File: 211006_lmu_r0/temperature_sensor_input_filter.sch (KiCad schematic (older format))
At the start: 4 parts

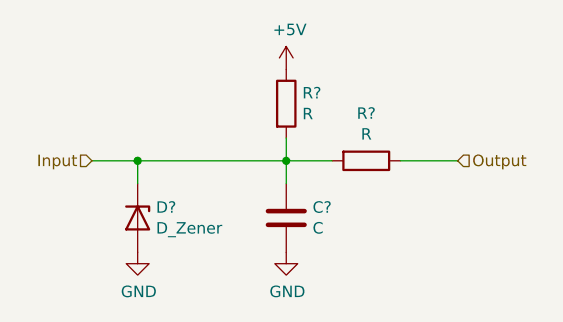
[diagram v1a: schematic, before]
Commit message: Updated BOM and footprints for non-hv components
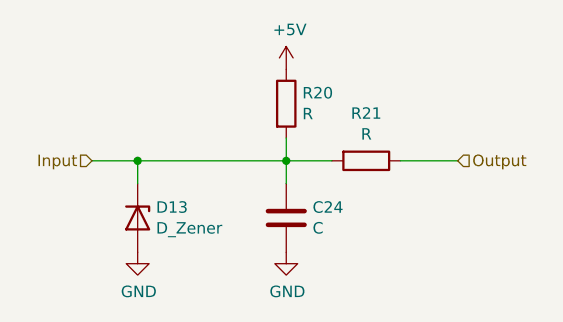
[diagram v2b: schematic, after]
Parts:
- gave numbers to parts that had none: 4
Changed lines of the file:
@@
 $EndDescr
 $Comp
-L Device:R R?
+L Device:R R6
 U 1 1 616C81A3
 P 6250 3350
-AR Path="/6171146A/616C8099/616C81A3" Ref="R?"  Part="1"
-AR Path="/6171146A/616CF5C8/616C81A3" Ref="R?"  Part="1"
-AR Path="/6171146A/616CF706/616C81A3" Ref="R?"  Part="1"
-AR Path="/6171146A/616CF70A/616C81A3" Ref="R?"  Part="1"
-AR Path="/6171146A/616D0104/616C81A3" Ref="R?"  Part="1"
-AR Path="/6171146A/616D0108/616C81A3" Ref="R?"  Part="1"
-AR Path="/6171146A/616D010C/616C81A3" Ref="R?"  Part="1"
-AR Path="/6171146A/616D0110/616C81A3" Ref="R?"  Part="1"
-F 0 "R?" H 6320 3396 50  0000 L CNN
+AR Path="/6171146A/616C8099/616C81A3" Ref="R6"  Part="1"
+AR Path="/6171146A/616CF5C8/616C81A3" Ref="R8"  Part="1"
+AR Path="/6171146A/616CF706/616C81A3" Ref="R10"  Part="1"
+AR Path="/6171146A/616CF70A/616C81A3" Ref="R12"  Part="1"
+AR Path="/6171146A/616D0104/616C81A3" Ref="R14"  Part="1"
+AR Path="/6171146A/616D0108/616C81A3" Ref="R16"  Part="1"
+AR Path="/6171146A/616D010C/616C81A3" Ref="R18"  Part="1"
+AR Path="/6171146A/616D0110/616C81A3" Ref="R20"  Part="1"
+F 0 "R20" H 6320 3396 50  0000 L CNN
 F 1 "R" H 6320 3305 50  0000 L CNN
 F 2 "" V 6180 3350 50  0001 C CNN
@@
 $EndComp
 $Comp
-L Device:R R?
+L Device:R R7
 U 1 1 616C83F1
 P 6600 3600
-AR Path="/6171146A/616C8099/616C83F1" Ref="R?"  Part="1"
-AR Path="/6171146A/616CF5C8/616C83F1" Ref="R?"  Part="1"
-AR Path="/6171146A/616CF706/616C83F1" Ref="R?"  Part="1"
-AR Path="/6171146A/616CF70A/616C83F1" Ref="R?"  Part="1"
-AR Path="/6171146A/616D0104/616C83F1" Ref="R?"  Part="1"
-AR Path="/6171146A/616D0108/616C83F1" Ref="R?"  Part="1"
-AR Path="/6171146A/616D010C/616C83F1" Ref="R?"  Part="1"
-AR Path="/6171146A/616D0110/616C83F1" Ref="R?"  Part="1"
-F 0 "R?" V 6393 3600 50  0000 C CNN
+AR Path="/6171146A/616C8099/616C83F1" Ref="R7"  Part="1"
+AR Path="/6171146A/616CF5C8/616C83F1" Ref="R9"  Part="1"
+AR Path="/6171146A/616CF706/616C83F1" Ref="R11"  Part="1"
+AR Path="/6171146A/616CF70A/616C83F1" Ref="R13"  Part="1"
+AR Path="/6171146A/616D0104/616C83F1" Ref="R15"  Part="1"
+AR Path="/6171146A/616D0108/616C83F1" Ref="R17"  Part="1"
+AR Path="/6171146A/616D010C/616C83F1" Ref="R19"  Part="1"
+AR Path="/6171146A/616D0110/616C83F1" Ref="R21"  Part="1"
+F 0 "R21" V 6393 3600 50  0000 C CNN
 F 1 "R" V 6484 3600 50  0000 C CNN
 F 2 "" V 6530 3600 50  0001 C CNN
@@
 $EndComp
 $Comp
-L Device:C C?
+L Device:C C17
 U 1 1 616C95FD
 P 6250 3850
-AR Path="/6171146A/616C8099/616C95FD" Ref="C?"  Part="1"
-AR Path="/6171146A/616CF5C8/616C95FD" Ref="C?"  Part="1"
-AR Path="/6171146A/616CF706/616C95FD" Ref="C?"  Part="1"
-AR Path="/6171146A/616CF70A/616C95FD" Ref="C?"  Part="1"
-AR Path="/6171146A/616D0104/616C95FD" Ref="C?"  Part="1"
-AR Path="/6171146A/616D0108/616C95FD" Ref="C?"  Part="1"
-AR Path="/6171146A/616D010C/616C95FD" Ref="C?"  Part="1"
-AR Path="/6171146A/616D0110/616C95FD" Ref="C?"  Part="1"
-F 0 "C?" H 6135 3804 50  0000 R CNN
+AR Path="/6171146A/616C8099/616C95FD" Ref="C17"  Part="1"
+AR Path="/6171146A/616CF5C8/616C95FD" Ref="C18"  Part="1"
+AR Path="/6171146A/616CF706/616C95FD" Ref="C19"  Part="1"
+AR Path="/6171146A/616CF70A/616C95FD" Ref="C20"  Part="1"
+AR Path="/6171146A/616D0104/616C95FD" Ref="C21"  Part="1"
+AR Path="/6171146A/616D0108/616C95FD" Ref="C22"  Part="1"
+AR Path="/6171146A/616D010C/616C95FD" Ref="C23"  Part="1"
+AR Path="/6171146A/616D0110/616C95FD" Ref="C24"  Part="1"
+F 0 "C24" H 6135 3804 50  0000 R CNN
 F 1 "C" H 6135 3895 50  0000 R CNN
 F 2 "" H 6288 3700 50  0001 C CNN
@@
 $EndComp
 $Comp
-L power:+5V #PWR?
+L power:+5V #PWR0116
 U 1 1 616CA1AB
 P 6250 3200
-AR Path="/6171146A/616C8099/616CA1AB" Ref="#PWR?"  Part="1"
-AR Path="/6171146A/616CF5C8/616CA1AB" Ref="#PWR?"  Part="1"
-AR Path="/6171146A/616CF706/616CA1AB" Ref="#PWR?"  Part="1"
-AR Path="/6171146A/616CF70A/616CA1AB" Ref="#PWR?"  Part="1"
-AR Path="/6171146A/616D0104/616CA1AB" Ref="#PWR?"  Part="1"
-AR Path="/6171146A/616D0108/616CA1AB" Ref="#PWR?"  Part="1"
-AR Path="/6171146A/616D010C/616CA1AB" Ref="#PWR?"  Part="1"
-AR Path="/6171146A/616D0110/616CA1AB" Ref="#PWR?"  Part="1"
-F 0 "#PWR?" H 6250 3050 50  0001 C CNN
+AR Path="/6171146A/616C8099/616CA1AB" Ref="#PWR0116"  Part="1"
+AR Path="/6171146A/616CF5C8/616CA1AB" Ref="#PWR0119"  Part="1"
+AR Path="/6171146A/616CF706/616CA1AB" Ref="#PWR0122"  Part="1"
+AR Path="/6171146A/616CF70A/616CA1AB" Ref="#PWR0125"  Part="1"
+AR Path="/6171146A/616D0104/616CA1AB" Ref="#PWR0128"  Part="1"
+AR Path="/6171146A/616D0108/616CA1AB" Ref="#PWR0131"  Part="1"
+AR Path="/6171146A/616D010C/616CA1AB" Ref="#PWR0134"  Part="1"
+AR Path="/6171146A/616D0110/616CA1AB" Ref="#PWR0137"  Part="1"
+F 0 "#PWR0137" H 6250 3050 50  0001 C CNN
 F 1 "+5V" H 6265 3373 50  0000 C CNN
 F 2 "" H 6250 3200 50  0001 C CNN
@@
 	6250 3600 6250 3700
 $Comp
-L power:GND #PWR?
+L power:GND #PWR0117
 U 1 1 616CAA95
 P 6250 4000
-AR Path="/6171146A/616C8099/616CAA95" Ref="#PWR?"  Part="1"
-AR Path="/6171146A/616CF5C8/616CAA95" Ref="#PWR?"  Part="1"
-AR Path="/6171146A/616CF706/616CAA95" Ref="#PWR?"  Part="1"
-AR Path="/6171146A/616CF70A/616CAA95" Ref="#PWR?"  Part="1"
-AR Path="/6171146A/616D0104/616CAA95" Ref="#PWR?"  Part="1"
-AR Path="/6171146A/616D0108/616CAA95" Ref="#PWR?"  Part="1"
-AR Path="/6171146A/616D010C/616CAA95" Ref="#PWR?"  Part="1"
-AR Path="/6171146A/616D0110/616CAA95" Ref="#PWR?"  Part="1"
-F 0 "#PWR?" H 6250 3750 50  0001 C CNN
+AR Path="/6171146A/616C8099/616CAA95" Ref="#PWR0117"  Part="1"
+AR Path="/6171146A/616CF5C8/616CAA95" Ref="#PWR0120"  Part="1"
+AR Path="/6171146A/616CF706/616CAA95" Ref="#PWR0123"  Part="1"
+AR Path="/6171146A/616CF70A/616CAA95" Ref="#PWR0126"  Part="1"
+AR Path="/6171146A/616D0104/616CAA95" Ref="#PWR0129"  Part="1"
+AR Path="/6171146A/616D0108/616CAA95" Ref="#PWR0132"  Part="1"
+AR Path="/6171146A/616D010C/616CAA95" Ref="#PWR0135"  Part="1"
+AR Path="/6171146A/616D0110/616CAA95" Ref="#PWR0138"  Part="1"
+F 0 "#PWR0138" H 6250 3750 50  0001 C CNN
 F 1 "GND" H 6255 3827 50  0000 C CNN
 F 2 "" H 6250 4000 50  0001 C CNN
@@
 $EndComp
 $Comp
-L Device:D_Zener D?
+L Device:D_Zener D6
 U 1 1 616CB2F4
 P 5600 3850
-AR Path="/6171146A/616C8099/616CB2F4" Ref="D?"  Part="1"
-AR Path="/6171146A/616CF5C8/616CB2F4" Ref="D?"  Part="1"
-AR Path="/6171146A/616CF706/616CB2F4" Ref="D?"  Part="1"
-AR Path="/6171146A/616CF70A/616CB2F4" Ref="D?"  Part="1"
-AR Path="/6171146A/616D0104/616CB2F4" Ref="D?"  Part="1"
-AR Path="/6171146A/616D0108/616CB2F4" Ref="D?"  Part="1"
-AR Path="/6171146A/616D010C/616CB2F4" Ref="D?"  Part="1"
-AR Path="/6171146A/616D0110/616CB2F4" Ref="D?"  Part="1"
-F 0 "D?" V 5554 3930 50  0000 L CNN
+AR Path="/6171146A/616C8099/616CB2F4" Ref="D6"  Part="1"
+AR Path="/6171146A/616CF5C8/616CB2F4" Ref="D7"  Part="1"
+AR Path="/6171146A/616CF706/616CB2F4" Ref="D8"  Part="1"
+AR Path="/6171146A/616CF70A/616CB2F4" Ref="D9"  Part="1"
+AR Path="/6171146A/616D0104/616CB2F4" Ref="D10"  Part="1"
+AR Path="/6171146A/616D0108/616CB2F4" Ref="D11"  Part="1"
+AR Path="/6171146A/616D010C/616CB2F4" Ref="D12"  Part="1"
+AR Path="/6171146A/616D0110/616CB2F4" Ref="D13"  Part="1"
+F 0 "D13" V 5554 3930 50  0000 L CNN
 F 1 "D_Zener" V 5645 3930 50  0000 L CNN
 F 2 "" H 5600 3850 50  0001 C CNN
@@
 $EndComp
 $Comp
-L power:GND #PWR?
+L power:GND #PWR0118
 U 1 1 616CBF3A
 P 5600 4000
-AR Path="/6171146A/616C8099/616CBF3A" Ref="#PWR?"  Part="1"
-AR Path="/6171146A/616CF5C8/616CBF3A" Ref="#PWR?"  Part="1"
-AR Path="/6171146A/616CF706/616CBF3A" Ref="#PWR?"  Part="1"
-AR Path="/6171146A/616CF70A/616CBF3A" Ref="#PWR?"  Part="1"
-AR Path="/6171146A/616D0104/616CBF3A" Ref="#PWR?"  Part="1"
-AR Path="/6171146A/616D0108/616CBF3A" Ref="#PWR?"  Part="1"
-AR Path="/6171146A/616D010C/616CBF3A" Ref="#PWR?"  Part="1"
-AR Path="/6171146A/616D0110/616CBF3A" Ref="#PWR?"  Part="1"
-F 0 "#PWR?" H 5600 3750 50  0001 C CNN
+AR Path="/6171146A/616C8099/616CBF3A" Ref="#PWR0118"  Part="1"
+AR Path="/6171146A/616CF5C8/616CBF3A" Ref="#PWR0121"  Part="1"
+AR Path="/6171146A/616CF706/616CBF3A" Ref="#PWR0124"  Part="1"
+AR Path="/6171146A/616CF70A/616CBF3A" Ref="#PWR0127"  Part="1"
+AR Path="/6171146A/616D0104/616CBF3A" Ref="#PWR0130"  Part="1"
+AR Path="/6171146A/616D0108/616CBF3A" Ref="#PWR0133"  Part="1"
+AR Path="/6171146A/616D010C/616CBF3A" Ref="#PWR0136"  Part="1"
+AR Path="/6171146A/616D0110/616CBF3A" Ref="#PWR0139"  Part="1"
+F 0 "#PWR0139" H 5600 3750 50  0001 C CNN
 F 1 "GND" H 5605 3827 50  0000 C CNN
 F 2 "" H 5600 4000 50  0001 C CNN

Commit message: Added most footprint requirements in HV
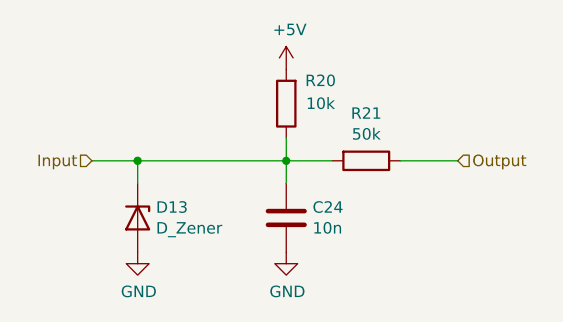
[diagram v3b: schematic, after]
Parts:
- C17: value C -> 10n; footprint (none) -> Capacitor_SMD:C_0603_1608Metric_Pad1.08x0.95mm_HandSolder
- D6: footprint (none) -> Diode_SMD:D_SMA_Handsoldering; Manufacturer (none) -> Diodes Inc; Part Number (none) -> SMAZ5V6-13-F
- R6: value R -> 10k; footprint (none) -> Resistor_SMD:R_0603_1608Metric_Pad0.98x0.95mm_HandSolder
- R7: value R -> 50k; footprint (none) -> Resistor_SMD:R_0603_1608Metric_Pad0.98x0.95mm_HandSolder
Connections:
- net +5V: now also R6.2; no longer R6.1
- net Input: now also R6.1; no longer R6.2
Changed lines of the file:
@@
 $EndDescr
-$Comp
-L Device:R R6
-U 1 1 616C81A3
-P 6250 3350
-AR Path="/6171146A/616C8099/616C81A3" Ref="R6"  Part="1"
-AR Path="/6171146A/616CF5C8/616C81A3" Ref="R8"  Part="1"
-AR Path="/6171146A/616CF706/616C81A3" Ref="R10"  Part="1"
-AR Path="/6171146A/616CF70A/616C81A3" Ref="R12"  Part="1"
-AR Path="/6171146A/616D0104/616C81A3" Ref="R14"  Part="1"
-AR Path="/6171146A/616D0108/616C81A3" Ref="R16"  Part="1"
-AR Path="/6171146A/616D010C/616C81A3" Ref="R18"  Part="1"
-AR Path="/6171146A/616D0110/616C81A3" Ref="R20"  Part="1"
-F 0 "R20" H 6320 3396 50  0000 L CNN
-F 1 "R" H 6320 3305 50  0000 L CNN
-F 2 "" V 6180 3350 50  0001 C CNN
-F 3 "~" H 6250 3350 50  0001 C CNN
-	1    6250 3350
-	1    0    0    -1
-$EndComp
 $Comp
 L Device:R R7
@@
 AR Path="/6171146A/616D0110/616C83F1" Ref="R21"  Part="1"
 F 0 "R21" V 6393 3600 50  0000 C CNN
-F 1 "R" V 6484 3600 50  0000 C CNN
-F 2 "" V 6530 3600 50  0001 C CNN
+F 1 "50k" V 6484 3600 50  0000 C CNN
+F 2 "Resistor_SMD:R_0603_1608Metric_Pad0.98x0.95mm_HandSolder" V 6530 3600 50  0001 C CNN
 F 3 "~" H 6600 3600 50  0001 C CNN
 	1    6600 3600
@@
 AR Path="/6171146A/616D0110/616C95FD" Ref="C24"  Part="1"
 F 0 "C24" H 6135 3804 50  0000 R CNN
-F 1 "C" H 6135 3895 50  0000 R CNN
-F 2 "" H 6288 3700 50  0001 C CNN
+F 1 "10n" H 6135 3895 50  0000 R CNN
+F 2 "Capacitor_SMD:C_0603_1608Metric_Pad1.08x0.95mm_HandSolder" H 6288 3700 50  0001 C CNN
 F 3 "~" H 6250 3850 50  0001 C CNN
 	1    6250 3850
@@
 $EndComp
 $Comp
-L power:+5V #PWR0116
+L power:+5V #PWR017
 U 1 1 616CA1AB
 P 6250 3200
-AR Path="/6171146A/616C8099/616CA1AB" Ref="#PWR0116"  Part="1"
-AR Path="/6171146A/616CF5C8/616CA1AB" Ref="#PWR0119"  Part="1"
-AR Path="/6171146A/616CF706/616CA1AB" Ref="#PWR0122"  Part="1"
-AR Path="/6171146A/616CF70A/616CA1AB" Ref="#PWR0125"  Part="1"
-AR Path="/6171146A/616D0104/616CA1AB" Ref="#PWR0128"  Part="1"
-AR Path="/6171146A/616D0108/616CA1AB" Ref="#PWR0131"  Part="1"
-AR Path="/6171146A/616D010C/616CA1AB" Ref="#PWR0134"  Part="1"
-AR Path="/6171146A/616D0110/616CA1AB" Ref="#PWR0137"  Part="1"
-F 0 "#PWR0137" H 6250 3050 50  0001 C CNN
+AR Path="/6171146A/616C8099/616CA1AB" Ref="#PWR017"  Part="1"
+AR Path="/6171146A/616CF5C8/616CA1AB" Ref="#PWR020"  Part="1"
+AR Path="/6171146A/616CF706/616CA1AB" Ref="#PWR023"  Part="1"
+AR Path="/6171146A/616CF70A/616CA1AB" Ref="#PWR026"  Part="1"
+AR Path="/6171146A/616D0104/616CA1AB" Ref="#PWR029"  Part="1"
+AR Path="/6171146A/616D0108/616CA1AB" Ref="#PWR032"  Part="1"
+AR Path="/6171146A/616D010C/616CA1AB" Ref="#PWR035"  Part="1"
+AR Path="/6171146A/616D0110/616CA1AB" Ref="#PWR038"  Part="1"
+F 0 "#PWR038" H 6250 3050 50  0001 C CNN
 F 1 "+5V" H 6265 3373 50  0000 C CNN
 F 2 "" H 6250 3200 50  0001 C CNN
@@
 	6250 3600 6250 3700
 $Comp
-L power:GND #PWR0117
+L power:GND #PWR018
 U 1 1 616CAA95
 P 6250 4000
-AR Path="/6171146A/616C8099/616CAA95" Ref="#PWR0117"  Part="1"
-AR Path="/6171146A/616CF5C8/616CAA95" Ref="#PWR0120"  Part="1"
-AR Path="/6171146A/616CF706/616CAA95" Ref="#PWR0123"  Part="1"
-AR Path="/6171146A/616CF70A/616CAA95" Ref="#PWR0126"  Part="1"
-AR Path="/6171146A/616D0104/616CAA95" Ref="#PWR0129"  Part="1"
-AR Path="/6171146A/616D0108/616CAA95" Ref="#PWR0132"  Part="1"
-AR Path="/6171146A/616D010C/616CAA95" Ref="#PWR0135"  Part="1"
-AR Path="/6171146A/616D0110/616CAA95" Ref="#PWR0138"  Part="1"
-F 0 "#PWR0138" H 6250 3750 50  0001 C CNN
+AR Path="/6171146A/616C8099/616CAA95" Ref="#PWR018"  Part="1"
+AR Path="/6171146A/616CF5C8/616CAA95" Ref="#PWR021"  Part="1"
+AR Path="/6171146A/616CF706/616CAA95" Ref="#PWR024"  Part="1"
+AR Path="/6171146A/616CF70A/616CAA95" Ref="#PWR027"  Part="1"
+AR Path="/6171146A/616D0104/616CAA95" Ref="#PWR030"  Part="1"
+AR Path="/6171146A/616D0108/616CAA95" Ref="#PWR033"  Part="1"
+AR Path="/6171146A/616D010C/616CAA95" Ref="#PWR036"  Part="1"
+AR Path="/6171146A/616D0110/616CAA95" Ref="#PWR039"  Part="1"
+F 0 "#PWR039" H 6250 3750 50  0001 C CNN
 F 1 "GND" H 6255 3827 50  0000 C CNN
 F 2 "" H 6250 4000 50  0001 C CNN
@@
 F 0 "D13" V 5554 3930 50  0000 L CNN
 F 1 "D_Zener" V 5645 3930 50  0000 L CNN
-F 2 "" H 5600 3850 50  0001 C CNN
+F 2 "Diode_SMD:D_SMA_Handsoldering" H 5600 3850 50  0001 C CNN
 F 3 "~" H 5600 3850 50  0001 C CNN
+F 4 "SMAZ5V6-13-F" V 5600 3850 50  0001 C CNN "Part Number"
+F 5 "Diodes Inc" V 5600 3850 50  0001 C CNN "Manufacturer"
 	1    5600 3850
 	0    1    1    0
 $EndComp
 $Comp
-L power:GND #PWR0118
+L power:GND #PWR016
 U 1 1 616CBF3A
 P 5600 4000
-AR Path="/6171146A/616C8099/616CBF3A" Ref="#PWR0118"  Part="1"
-AR Path="/6171146A/616CF5C8/616CBF3A" Ref="#PWR0121"  Part="1"
-AR Path="/6171146A/616CF706/616CBF3A" Ref="#PWR0124"  Part="1"
-AR Path="/6171146A/616CF70A/616CBF3A" Ref="#PWR0127"  Part="1"
-AR Path="/6171146A/616D0104/616CBF3A" Ref="#PWR0130"  Part="1"
-AR Path="/6171146A/616D0108/616CBF3A" Ref="#PWR0133"  Part="1"
-AR Path="/6171146A/616D010C/616CBF3A" Ref="#PWR0136"  Part="1"
-AR Path="/6171146A/616D0110/616CBF3A" Ref="#PWR0139"  Part="1"
-F 0 "#PWR0139" H 5600 3750 50  0001 C CNN
+AR Path="/6171146A/616C8099/616CBF3A" Ref="#PWR016"  Part="1"
+AR Path="/6171146A/616CF5C8/616CBF3A" Ref="#PWR019"  Part="1"
+AR Path="/6171146A/616CF706/616CBF3A" Ref="#PWR022"  Part="1"
+AR Path="/6171146A/616CF70A/616CBF3A" Ref="#PWR025"  Part="1"
+AR Path="/6171146A/616D0104/616CBF3A" Ref="#PWR028"  Part="1"
+AR Path="/6171146A/616D0108/616CBF3A" Ref="#PWR031"  Part="1"
+AR Path="/6171146A/616D010C/616CBF3A" Ref="#PWR034"  Part="1"
+AR Path="/6171146A/616D0110/616CBF3A" Ref="#PWR037"  Part="1"
+F 0 "#PWR037" H 5600 3750 50  0001 C CNN
 F 1 "GND" H 5605 3827 50  0000 C CNN
 F 2 "" H 5600 4000 50  0001 C CNN
@@
 Text HLabel 5400 3600 0    50   Input ~ 0
 Input
+$Comp
+L Device:R R6
+U 1 1 61F70D2C
+P 6250 3350
+AR Path="/6171146A/616C8099/61F70D2C" Ref="R6"  Part="1"
+AR Path="/6171146A/616CF5C8/61F70D2C" Ref="R8"  Part="1"
+AR Path="/6171146A/616CF706/61F70D2C" Ref="R10"  Part="1"
+AR Path="/6171146A/616CF70A/61F70D2C" Ref="R12"  Part="1"
+AR Path="/6171146A/616D0104/61F70D2C" Ref="R14"  Part="1"
+AR Path="/6171146A/616D0108/61F70D2C" Ref="R16"  Part="1"
+AR Path="/6171146A/616D010C/61F70D2C" Ref="R18"  Part="1"
+AR Path="/6171146A/616D0110/61F70D2C" Ref="R20"  Part="1"
+F 0 "R20" H 6100 3250 50  0000 C CNN
+F 1 "10k" H 6100 3350 50  0000 C CNN
+F 2 "Resistor_SMD:R_0603_1608Metric_Pad0.98x0.95mm_HandSolder" V 6180 3350 50  0001 C CNN
+F 3 "~" H 6250 3350 50  0001 C CNN
+	1    6250 3350
+	-1   0    0    1
+$EndComp
 $EndSCHEMATC

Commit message: Updated with Mouser links for BOM
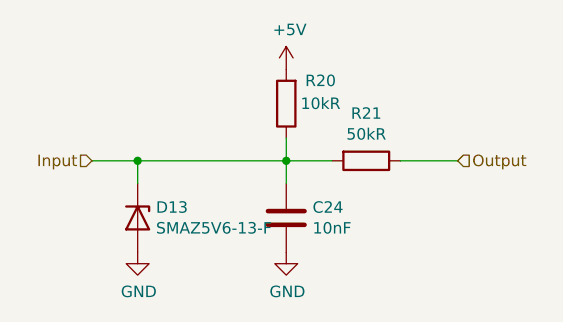
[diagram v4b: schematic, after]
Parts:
- C17: value 10n -> 10nF
- D6: value D_Zener -> SMAZ5V6-13-F; Mouser Part Number (none) -> NOT AVAILABLE!; Mouser URL (none) -> NOT AVAILABLE!
- R6: value 10k -> 10kR
- R7: value 50k -> 50kR
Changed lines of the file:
@@
 AR Path="/6171146A/616D0110/616C83F1" Ref="R21"  Part="1"
 F 0 "R21" V 6393 3600 50  0000 C CNN
-F 1 "50k" V 6484 3600 50  0000 C CNN
+F 1 "50kR" V 6484 3600 50  0000 C CNN
 F 2 "Resistor_SMD:R_0603_1608Metric_Pad0.98x0.95mm_HandSolder" V 6530 3600 50  0001 C CNN
 F 3 "~" H 6600 3600 50  0001 C CNN
@@
 AR Path="/6171146A/616D0110/616C95FD" Ref="C24"  Part="1"
 F 0 "C24" H 6135 3804 50  0000 R CNN
-F 1 "10n" H 6135 3895 50  0000 R CNN
+F 1 "10nF" H 6135 3895 50  0000 R CNN
 F 2 "Capacitor_SMD:C_0603_1608Metric_Pad1.08x0.95mm_HandSolder" H 6288 3700 50  0001 C CNN
 F 3 "~" H 6250 3850 50  0001 C CNN
@@
 AR Path="/6171146A/616D0110/616CB2F4" Ref="D13"  Part="1"
 F 0 "D13" V 5554 3930 50  0000 L CNN
-F 1 "D_Zener" V 5645 3930 50  0000 L CNN
+F 1 "SMAZ5V6-13-F" V 5645 3930 50  0000 L CNN
 F 2 "Diode_SMD:D_SMA_Handsoldering" H 5600 3850 50  0001 C CNN
 F 3 "~" H 5600 3850 50  0001 C CNN
 F 4 "SMAZ5V6-13-F" V 5600 3850 50  0001 C CNN "Part Number"
 F 5 "Diodes Inc" V 5600 3850 50  0001 C CNN "Manufacturer"
+F 6 "NOT AVAILABLE!" H 5600 3850 50  0001 C CNN "Mouser Part Number"
+F 7 "NOT AVAILABLE!" H 5600 3850 50  0001 C CNN "Mouser URL"
 	1    5600 3850
 	0    1    1    0
@@
 AR Path="/6171146A/616D0110/61F70D2C" Ref="R20"  Part="1"
 F 0 "R20" H 6100 3250 50  0000 C CNN
-F 1 "10k" H 6100 3350 50  0000 C CNN
+F 1 "10kR" H 6100 3350 50  0000 C CNN
 F 2 "Resistor_SMD:R_0603_1608Metric_Pad0.98x0.95mm_HandSolder" V 6180 3350 50  0001 C CNN
 F 3 "~" H 6250 3350 50  0001 C CNN
